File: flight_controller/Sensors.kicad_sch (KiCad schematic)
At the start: 21 parts, among them U16 FM25V02A-GTR, U17 MS561101BA03-50, U18 MPU6500, U19 W25Q512JVFIQ

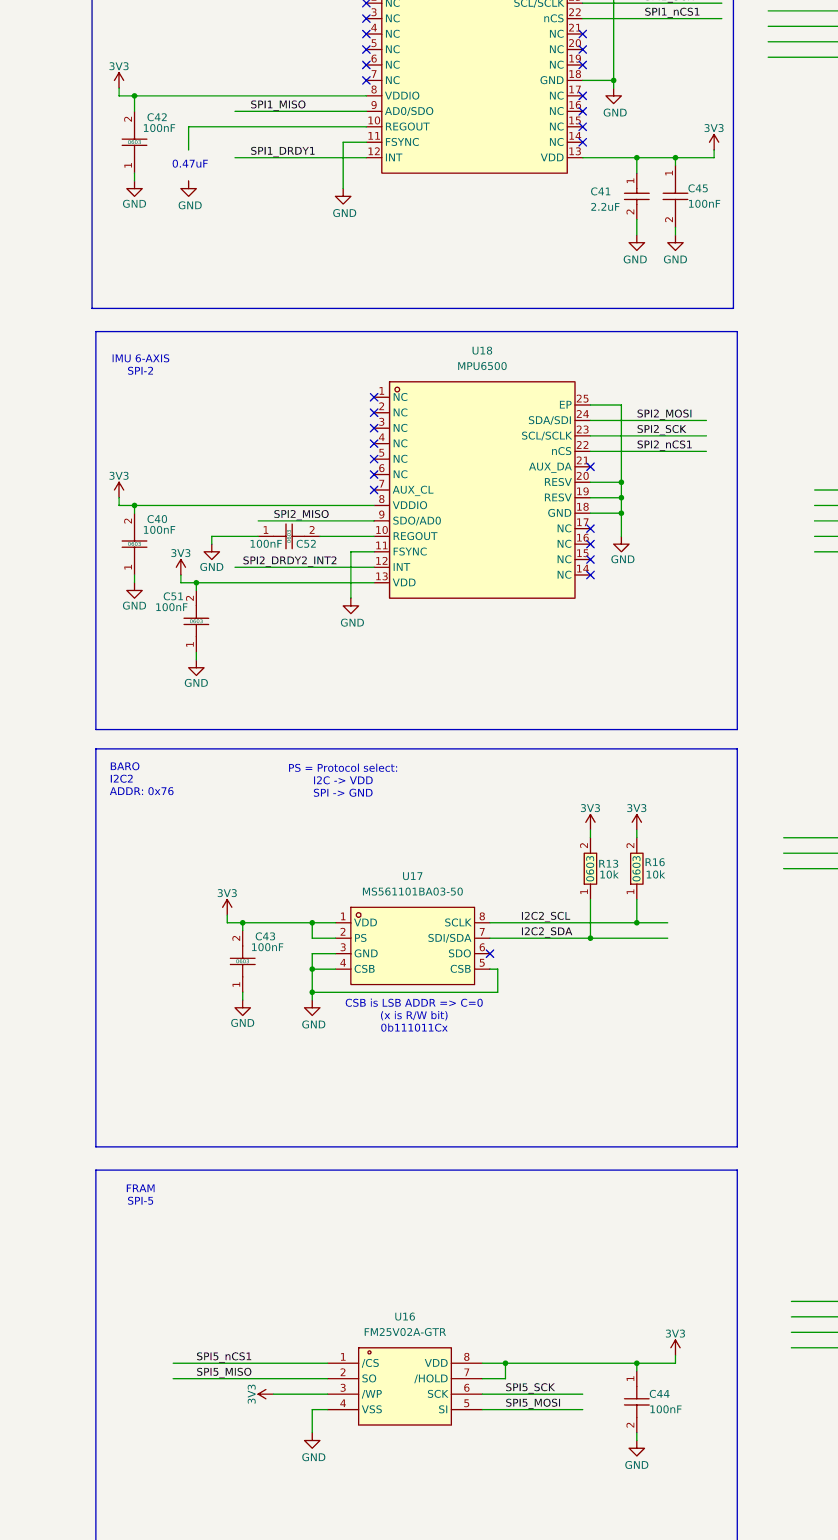
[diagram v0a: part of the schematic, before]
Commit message: updating symbols as in the shared library
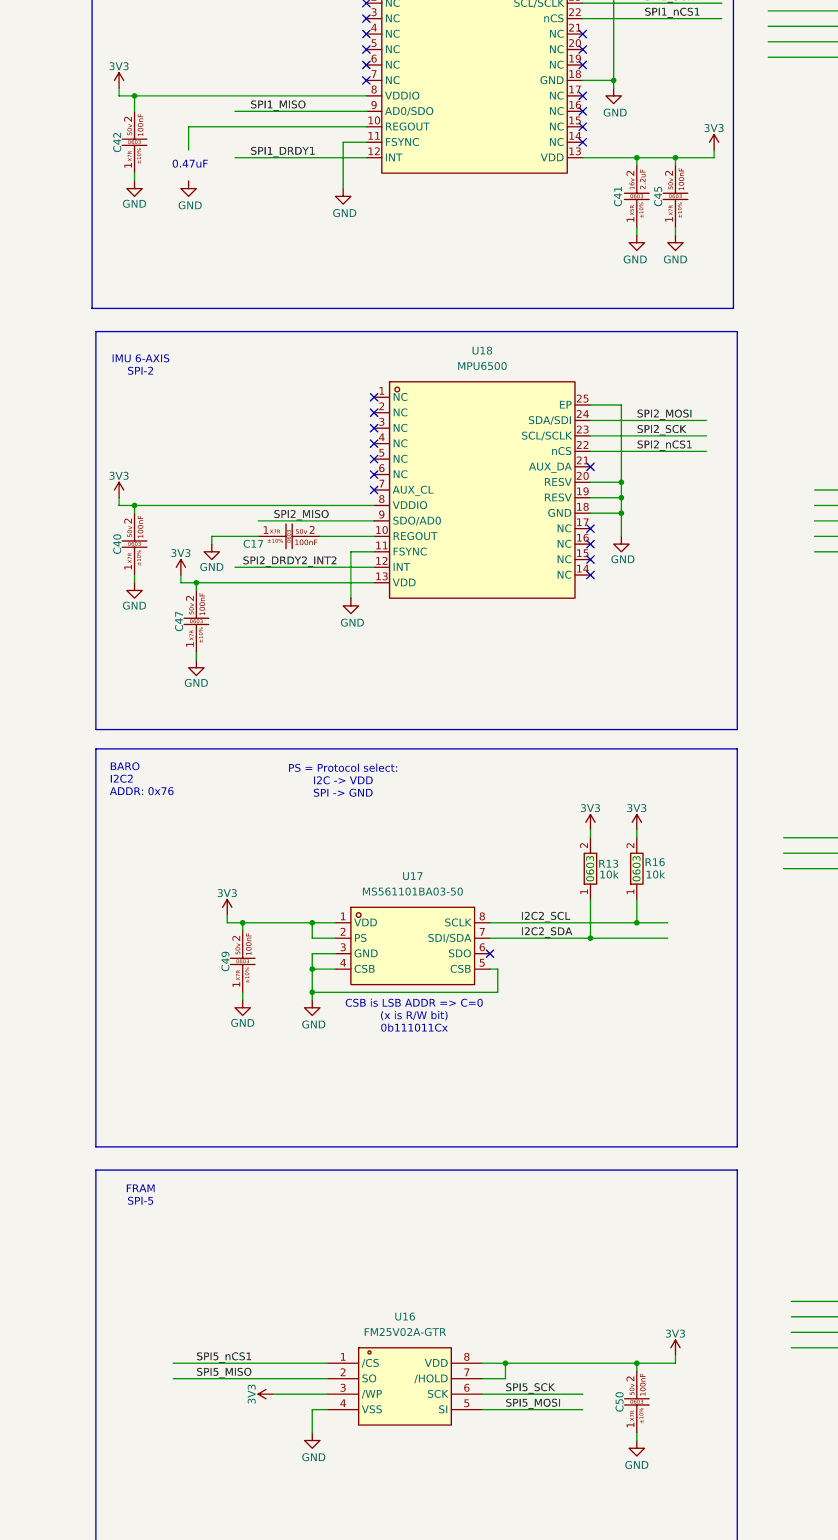
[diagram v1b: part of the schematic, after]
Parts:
- removed C40, C42, C43, C51, C52: CC0603KRX7R9BB104, easyeda2kicad:C0603, symbol easyeda2kicad:CC0603KRX7R9BB104
- removed C41: GRM155R61A225KE95D, easyeda2kicad:C0402, symbol easyeda2kicad:GRM155R61A225KE95D
- removed C44, C45: CC0402JRX7R7BB104, easyeda2kicad:C0402, symbol easyeda2kicad:CC0402JRX7R7BB104
- added C17, C40, C42, C45, C47, C49, C50: CC0603KRX7R9BB104 (100nf , 0603 ,50v ,X7R), easyeda2kicad:C0603, symbol lampelKicadLIB:CC0603KRX7R9BB104 (100nf , 0603 ,50v ,X7R)
- added C41: CL10A225KO8NNNC (2.2uf , 0603,16v,X5R), easyeda2kicad:C0603, symbol lampelKicadLIB:CL10A225KO8NNNC (2.2uf , 0603,16v,X5R)
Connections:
- net 3V3: now also C40.2, C41.2, C42.2, C45.2, C47.2, C49.2, C50.2
- net GND: now also C17.1, C40.1, C41.1, C42.1, C45.1, C47.1, C49.1, C50.1
- net at U18.10 (REGOUT): now also C17.2

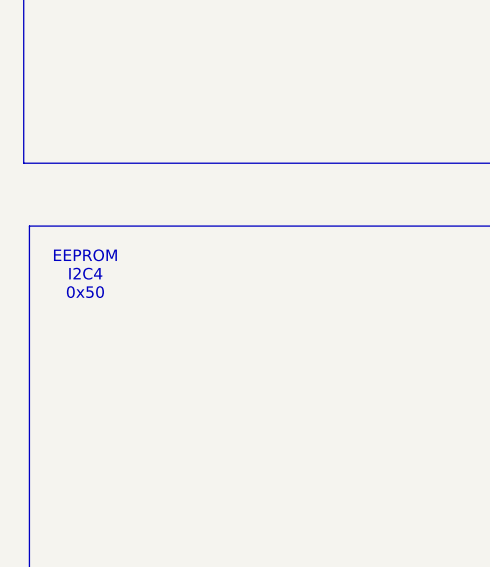
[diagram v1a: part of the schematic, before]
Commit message: update debug conn
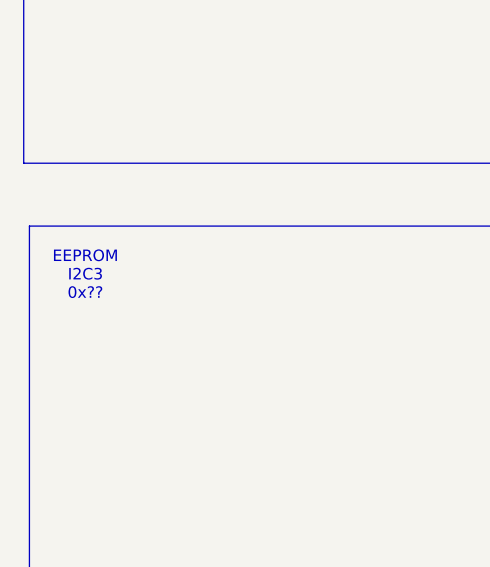
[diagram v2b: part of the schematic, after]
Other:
- note added: "EEPROM I2C3 0x??"
- note removed: "EEPROM I2C4 0x50"
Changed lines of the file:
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@@
 		)
 	)
-	(text "EEPROM\nI2C4\n0x50"
+	(text "EEPROM\nI2C3\n0x??"
 		(exclude_from_sim no)
 		(at 108.458 180.848 0)

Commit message: ALL CONNECTORS, ETH, SERVO,RC,SPI,FLASH and more. to finish GPSand STM32 PINOUT
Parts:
- added C55, C58: CC0603KRX7R9BB104 (100nf , 0603 ,50v ,X7R), easyeda2kicad:C0603, symbol lampelKicadLIB:CC0603KRX7R9BB104 (100nf , 0603 ,50v ,X7R)
- added R86: 0603WAF1002T5E, easyeda2kicad:R0603, symbol easyeda2kicad:0603WAF1002T5E
- added U4: 24LC64-I/SN, easyeda2kicad:SOIC-8_L4.9-W3.9-P1.27-LS6.0-BL, symbol lampelKicadLIB:24LC64-I_SN
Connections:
- net 3V3: now also U19.2 (VCC), U19.3 (~{RESET}), C55.2, C58.2, R86.2, U4.1 (A0), U4.8 (VCC)
- net GND: now also U19.10 (GND), C55.1, C58.1, U4.2 (A1), U4.3 (A2), U4.4 (VSS), U4.7 (WP)
- net QUADSPI_BK1_IO3: now reaches U19.1 (HOLD#orRESET#(IO3))
- net QUADSPI_BK1_IO0: now reaches U19.15 (DI(IO0))
- net QUADSPI_CLK: now reaches U19.16 (CLK)
- net QUADSPI_BK1_NCS: now reaches U19.7 (~{CS})
- net QUADSPI_BK1_NCS: now also R86.1
- net QUADSPI_BK1_IO1: now reaches U19.8 (DO(IO1))
- net QUADSPI_BK1_IO2: now reaches U19.9 (WP#(IO2))
- new net I2C3_SCL_EEPROM: U4.6 (SCL)
- new net I2C3_SDA_EEPROM: U4.5 (SDA)
- no-connect marks 31 -> 38
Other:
- note added: "EEPROM 64Kbit I2C3 - 0x51"
- note removed: "EEPROM I2C3 0x??"
- moved on the sheet: C49, Card1, R13, R14, R15, R16, R17, R18, R19, U17, U19

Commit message: cleanup and improvements
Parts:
- added C53: CC0603KRX7R9BB474 (470nF , 0603 ,50V ,X7R), easyeda2kicad:C0603, symbol lampelKicadLIB:CC0603KRX7R9BB474 (470nF , 0603 ,50V ,X7R)
- added C72: CC0603KRX7R9BB104 (100nf , 0603 ,50v ,X7R), easyeda2kicad:C0603, symbol lampelKicadLIB:CC0603KRX7R9BB104 (100nf , 0603 ,50v ,X7R)
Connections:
- net 3V3: now also C72.2
- net GND: now also C53.1, C72.1
- net at R8.10 (REGOUT): now also C53.2
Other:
- note removed: "0.47uF"

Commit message: Started the placement process
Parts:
- removed Card1: TF PUSH, easyeda2kicad:TF-SMD_TF-PUSH, symbol easyeda_symbole:TFPUSH
- added Card1: TFPUSH (Micro SD card), easyeda2kicad:TF-SMD_TF-PUSH, symbol easyeda_lampel:TFPUSH (Micro SD card)
- renumbered C58 to C48, C72 to C49, C55 to C50, C42 to C51, C40 to C52, C47 to C54, C17 to C55, C49 to C56, C41 to C57, C50 to C58, C45 to C59, R17 to R50, R86 to R51, R14 to R52, R18 to R53, R15 to R54, R19 to R55, R8 to R56, R13 to R57, R16 to R58, U4 to U10, U16 to U11, U18 to U12, U17 to U13, U19 to U9
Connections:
- net 3V3: now also Card1.4 (VDD)
- net GND: now also Card1.6 (VSS)
- net SDMMC2_CLK: now also Card1.5 (CLX)
- net SDMMC2_CMD: now also Card1.3 (CMD)
- net SDMMC2_D0: now also Card1.7 (DAT0)
- net SDMMC2_D1: now also Card1.8 (DAT1)
- net SDMMC2_D2: now also Card1.1 (DAT2)
- net SDMMC2_D3: now also Card1.2 (CD/DAT3)
- net SD_CARD_DETECT: now also Card1.9 (CD)

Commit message: Almost done with placement , fixed some 3d models , fixed r56 to u56
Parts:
- renumbered R56 to U56
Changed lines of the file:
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@@
 		(dnp no)
 		(fields_autoplaced yes)
-		(property "Reference" "R56"
+		(property "Reference" "U56"
 			(at 408.94 50.8 0)
 			(effects
@@
 			(project "FP_BOARD"
 				(path "/17737359-1a8e-4237-8899-d9604030bc1d/868a4ffc-d89e-48bc-9c7c-6b44894a914b"
-					(reference "R56")
+					(reference "U56")
 					(unit 1)
 				)

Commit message: Advanced in routing
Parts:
- removed Card1: TFPUSH (Micro SD card), easyeda2kicad:TF-SMD_TF-PUSH, symbol easyeda_lampel:TFPUSH (Micro SD card)
- added Card2: TF-01A, easyeda2kicad:TF-SMD_TF-01A, symbol easyeda_lampel:TF-01A
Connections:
- net 3V3: now also Card2.4 (VDD)
- net GND: now also Card2.10 (GND), Card2.11 (GND), Card2.12 (GND), Card2.13 (GND), Card2.6 (VSS)
- net SDMMC2_CLK: now also Card2.5 (CLK(SCLK))
- net SDMMC2_CMD: now also Card2.3 (CMD(DI))
- net SDMMC2_D0: now also Card2.7 (DAT0(D0))
- net SDMMC2_D1: now also Card2.8 (DAT1(RSV))
- net SDMMC2_D2: now also Card2.1 (DAT2(RSV))
- net SDMMC2_D3: now also Card2.2 (CDDAT3(CS))
- net SD_CARD_DETECT: now also Card2.9 (CD)
- no-connect marks 38 -> 34

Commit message: Almost finish with initial routing
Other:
- moved on the sheet: C59
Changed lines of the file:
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@@
 	(symbol
 		(lib_id "lampelKicadLIB:CC0603KRX7R9BB104 (100nf , 0603 ,50v ,X7R)")
-		(at 441.96 95.25 90)
+		(at 441.96 95.25 270)
+		(mirror x)
 		(unit 1)
 		(exclude_from_sim no)
@@
 		(on_board yes)
 		(dnp no)
-		(fields_autoplaced yes)
 		(property "Reference" "C59"
-			(at 439.166 95.25 0)
+			(at 444.754 95.25 0)
 			(do_not_autoplace yes)
 			(effects
@@
 		)
 		(property "Value" "CC0603KRX7R9BB104 (100nf , 0603 ,50v ,X7R)"
-			(at 447.04 95.25 0)
+			(at 436.88 95.25 0)
 			(effects
 				(font
@@
 		)
 		(property "Footprint" "easyeda2kicad:C0603"
-			(at 449.58 95.25 0)
+			(at 434.34 95.25 0)
 			(effects
 				(font
@@
 		)
 		(property "Datasheet" "https://lcsc.com/product-detail/Multilayer-Ceramic-Capacitors-MLCC-SMD-SMT_100nF-104-10-50V_C14663.html"
-			(at 452.12 95.25 0)
+			(at 431.8 95.25 0)
 			(effects
 				(font
@@
 		)
 		(property "LCSC Part" "C14663"
-			(at 454.66 95.25 0)
+			(at 429.26 95.25 0)
 			(effects
 				(font
